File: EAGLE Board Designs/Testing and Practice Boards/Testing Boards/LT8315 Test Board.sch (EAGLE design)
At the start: 21 parts, among them T1 TRANSFORMER(3W), U1 LT8315

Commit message: Finished schem and started board
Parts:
- added C10, C9: CAPACITOR_1206_25V_33UF, HyTechDevices:CAPACITOR_1206_25V_33UF
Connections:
- net N$15: now also C10.1, C9.1
- net N$16: now also C10.2, C9.2
- net N$2: no longer C8.2
- net TS-UNFUSED: now also C8.2
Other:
- moved on the sheet: C8
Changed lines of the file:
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@@
 <part name="C7" library="HyTechDevices" deviceset="CAPACITOR_?_*" device="0603" technology="100V_0.1UF"/>
 <part name="C8" library="HyTechDevices" deviceset="CAPACITOR_?_*" device="" technology="0.1UF"/>
+<part name="C9" library="HyTechDevices" deviceset="CAPACITOR_?_*" device="1206" technology="25V_33UF"/>
+<part name="C10" library="HyTechDevices" deviceset="CAPACITOR_?_*" device="1206" technology="25V_33UF"/>
+<part name="P4" library="HyTechSupplies" deviceset="TS+UNFUSED" device=""/>
+<part name="P5" library="HyTechSupplies" deviceset="TS-UNFUSED" device=""/>
 </parts>
 <sheets>
@@
 <attribute name="CAPACITANCE" x="249.428" y="142.24" size="1.27" layer="96" rot="R90" align="top-center"/>
 </instance>
-<instance part="C8" gate="G$1" x="186.69" y="138.43" smashed="yes" rot="R90">
-<attribute name="NAME" x="184.15" y="137.16" size="1.27" layer="95" rot="R90" align="bottom-center"/>
+<instance part="C8" gate="G$1" x="60.96" y="139.7" smashed="yes" rot="R90">
+<attribute name="NAME" x="58.42" y="138.43" size="1.27" layer="95" rot="R90" align="bottom-center"/>
+</instance>
+<instance part="C9" gate="G$1" x="255.27" y="143.51" smashed="yes" rot="R90">
+<attribute name="NAME" x="252.73" y="142.24" size="1.27" layer="95" rot="R90" align="bottom-center"/>
+<attribute name="VOLTAGE" x="257.81" y="142.24" size="1.27" layer="96" rot="R90" align="top-center"/>
+<attribute name="CAPACITANCE" x="259.588" y="142.24" size="1.27" layer="96" rot="R90" align="top-center"/>
+</instance>
+<instance part="C10" gate="G$1" x="265.43" y="143.51" smashed="yes" rot="R90">
+<attribute name="NAME" x="262.89" y="142.24" size="1.27" layer="95" rot="R90" align="bottom-center"/>
+<attribute name="VOLTAGE" x="267.97" y="142.24" size="1.27" layer="96" rot="R90" align="top-center"/>
+<attribute name="CAPACITANCE" x="269.748" y="142.24" size="1.27" layer="96" rot="R90" align="top-center"/>
+</instance>
+<instance part="P4" gate="G$1" x="60.96" y="147.32" smashed="yes">
+<attribute name="VALUE" x="60.96" y="152.4" size="1.27" layer="96" align="bottom-center"/>
+</instance>
+<instance part="P5" gate="G$1" x="60.96" y="129.54" smashed="yes">
+<attribute name="VALUE" x="60.96" y="127" size="1.27" layer="96" align="top-center"/>
 </instance>
 </instances>
@@
 <wire x1="177.8" y1="132.08" x2="156.21" y2="132.08" width="0.1524" layer="91"/>
 <junction x="177.8" y="132.08"/>
-<pinref part="C8" gate="G$1" pin="2"/>
-<wire x1="186.69" y1="133.35" x2="186.69" y2="132.08" width="0.1524" layer="91"/>
-<junction x="186.69" y="132.08"/>
 </segment>
 </net>
@@
 <wire x1="182.88" y1="142.24" x2="186.69" y2="142.24" width="0.1524" layer="91"/>
 <pinref part="T1" gate="G$1" pin="3"/>
+<wire x1="186.69" y1="142.24" x2="189.23" y2="142.24" width="0.1524" layer="91"/>
+</segment>
+<segment>
+<pinref part="P4" gate="G$1" pin="TS+UNFUSED"/>
 <pinref part="C8" gate="G$1" pin="1"/>
-<wire x1="186.69" y1="142.24" x2="189.23" y2="142.24" width="0.1524" layer="91"/>
-<wire x1="186.69" y1="140.97" x2="186.69" y2="142.24" width="0.1524" layer="91"/>
-<junction x="186.69" y="142.24"/>
+<wire x1="60.96" y1="142.24" x2="60.96" y2="144.78" width="0.1524" layer="91"/>
 </segment>
 </net>
@@
 <wire x1="171.45" y1="157.48" x2="184.15" y2="157.48" width="0.1524" layer="91"/>
 </segment>
+<segment>
+<pinref part="P5" gate="G$1" pin="TS-UNFUSED"/>
+<pinref part="C8" gate="G$1" pin="2"/>
+<wire x1="60.96" y1="132.08" x2="60.96" y2="134.62" width="0.1524" layer="91"/>
+</segment>
 </net>
 <net name="N$4" class="0">
@@
 <wire x1="245.11" y1="147.32" x2="245.11" y2="146.05" width="0.1524" layer="91"/>
 <junction x="234.95" y="147.32"/>
+<pinref part="C9" gate="G$1" pin="1"/>
+<wire x1="245.11" y1="147.32" x2="255.27" y2="147.32" width="0.1524" layer="91"/>
+<wire x1="255.27" y1="147.32" x2="255.27" y2="146.05" width="0.1524" layer="91"/>
+<junction x="245.11" y="147.32"/>
+<pinref part="C10" gate="G$1" pin="1"/>
+<wire x1="255.27" y1="147.32" x2="265.43" y2="147.32" width="0.1524" layer="91"/>
+<wire x1="265.43" y1="147.32" x2="265.43" y2="146.05" width="0.1524" layer="91"/>
+<junction x="255.27" y="147.32"/>
 </segment>
 </net>
@@
 <wire x1="245.11" y1="137.16" x2="234.95" y2="137.16" width="0.1524" layer="91"/>
 <junction x="234.95" y="137.16"/>
-</segment>
-</net>
+<pinref part="C9" gate="G$1" pin="2"/>
+<wire x1="245.11" y1="137.16" x2="255.27" y2="137.16" width="0.1524" layer="91"/>
+<wire x1="255.27" y1="137.16" x2="255.27" y2="138.43" width="0.1524" layer="91"/>
+<junction x="245.11" y="137.16"/>
+<pinref part="C10" gate="G$1" pin="2"/>
+<wire x1="255.27" y1="137.16" x2="265.43" y2="137.16" width="0.1524" layer="91"/>
+<wire x1="265.43" y1="137.16" x2="265.43" y2="138.43" width="0.1524" layer="91"/>
+<junction x="255.27" y="137.16"/>
+</segment>
+</net>

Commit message: Made more changes to board and schematic
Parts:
- added D5: LED_0603_GREEN, HyTechDevices:LED_0603_GREEN
- added J1, J2: CONNECTOR-2_μF_T_V_BLACK, HyTechDevices:CONNECTOR-2_μF_T_V_BLACK
- added R8: RESISTOR_0603_1K, HyTechDevices:RESISTOR_0603_1K
- added TP1, TP2, TP3, TP4, TP5: TEST_POINT, HyTechDevices:TEST_POINT
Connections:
- removed net N$16: C10.2, C6.2, C7.2, C9.2, T1.10,11
- new net +5V: C10.1, C6.1, C7.1, C9.1, D4.C, J2.1, R8.2, TP4.1
- new net GND: C10.2, C6.2, C7.2, C9.2, D5.C, J2.2, T1.10,11, TP5.1
- net N$15: now also D5.A, R8.1; no longer C10.1, C6.1, C7.1, C9.1, D4.C
- net N$9: now also TP1.1
- net TS+UNFUSED: now also J1.1, TP2.1
- net TS-UNFUSED: now also J1.2, TP3.1
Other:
- moved on the sheet: C1, C10, C2, C3, C4, C5, C6, C7, C8, C9, D1, D2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

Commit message: Added BOMs and finished board
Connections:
- net +5V renamed +12V
- net N$9 renamed AUX
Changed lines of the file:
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@@
 <part name="U1" library="HyTechDevices" deviceset="LT8315" device=""/>
 <part name="D1" library="HyTechDevices" deviceset="TVS_*" device="SOD323F"/>
-<part name="D2" library="HyTechDevices" deviceset="RECTIFIER_*_?" device="SMA"/>
 <part name="T1" library="HyTechDevices" deviceset="TRANSFORMER(3W)" device=""/>
 <part name="P1" library="HyTechSupplies" deviceset="TS-UNFUSED" device=""/>
@@
 <part name="TP4" library="HyTechDevices" deviceset="TEST_POINT" device=""/>
 <part name="TP5" library="HyTechDevices" deviceset="TEST_POINT" device=""/>
-<part name="P6" library="HyTechSupplies" deviceset="+5V" device=""/>
 <part name="P7" library="HyTechSupplies" deviceset="GND" device=""/>
-<part name="P8" library="HyTechSupplies" deviceset="+5V" device=""/>
 <part name="P9" library="HyTechSupplies" deviceset="GND" device=""/>
 <part name="R8" library="HyTechDevices" deviceset="RESISTOR_?_*" device="0603" technology="1K"/>
 <part name="D5" library="HyTechDevices" deviceset="LED_?_*" device="0603" technology="GREEN"/>
+<part name="P6" library="HyTechSupplies" deviceset="+12V" device=""/>
+<part name="P8" library="HyTechSupplies" deviceset="+12V" device=""/>
+<part name="D2" library="HyTechDevices" deviceset="RECTIFIER_*_?" device="SMA"/>
 </parts>
 <sheets>
@@
 <attribute name="VOLTAGE" x="147.955" y="140.97" size="1.27" layer="96" rot="R270" align="top-center"/>
 </instance>
-<instance part="D2" gate="G$1" x="149.86" y="134.62" smashed="yes" rot="R90">
-<attribute name="NAME" x="147.955" y="133.35" size="1.27" layer="95" rot="R90" align="bottom-center"/>
-<attribute name="MPN" x="153.67" y="133.35" size="1.27" layer="96" rot="R90" align="top-center"/>
-</instance>
 <instance part="T1" gate="G$1" x="173.99" y="139.7" smashed="yes">
 <attribute name="NAME" x="173.99" y="150.622" size="1.27" layer="95" align="bottom-center"/>
@@
 <attribute name="MPN" x="245.618" y="129.54" size="1.27" layer="95" rot="R90" align="top-left"/>
 </instance>
-<instance part="P6" gate="1" x="217.17" y="147.32" smashed="yes">
-<attribute name="VALUE" x="217.17" y="149.86" size="1.27" layer="96" align="bottom-center"/>
-</instance>
 <instance part="P7" gate="1" x="217.17" y="132.08" smashed="yes">
 <attribute name="VALUE" x="217.17" y="130.81" size="1.27" layer="96" align="top-center"/>
-</instance>
-<instance part="P8" gate="1" x="217.17" y="124.46" smashed="yes">
-<attribute name="VALUE" x="217.17" y="127" size="1.27" layer="96" align="bottom-center"/>
 </instance>
 <instance part="P9" gate="1" x="217.17" y="104.14" smashed="yes">
@@
 <attribute name="COLOR" x="215.392" y="110.49" size="1.27" layer="95" rot="R270" align="top-center"/>
 <attribute name="NAME" x="220.726" y="110.49" size="1.27" layer="96" rot="R270" align="bottom-center"/>
+</instance>
+<instance part="P6" gate="1" x="217.17" y="124.46" smashed="yes">
+<attribute name="VALUE" x="217.17" y="128.27" size="1.27" layer="96" align="bottom-center"/>
+</instance>
+<instance part="P8" gate="1" x="217.17" y="147.066" smashed="yes">
+<attribute name="VALUE" x="217.17" y="150.876" size="1.27" layer="96" align="bottom-center"/>
+</instance>
+<instance part="D2" gate="G$1" x="149.86" y="134.62" smashed="yes" rot="R90">
+<attribute name="NAME" x="147.955" y="133.35" size="1.27" layer="95" rot="R90" align="bottom-center"/>
+<attribute name="VOLTAGE" x="151.765" y="133.35" size="1.27" layer="96" rot="R90" align="top-center"/>
+<attribute name="MPN" x="153.67" y="133.35" size="1.27" layer="96" rot="R90" align="top-center"/>
 </instance>
 </instances>
@@
 </busses>
 <nets>
-<net name="N$1" class="0">
-<segment>
-<pinref part="D2" gate="G$1" pin="C"/>
-<pinref part="D1" gate="G$1" pin="C"/>
-</segment>
-</net>
 <net name="N$2" class="0">
 <segment>
 <pinref part="T1" gate="G$1" pin="1"/>
-<pinref part="D2" gate="G$1" pin="A"/>
 <pinref part="U1" gate="G$1" pin="DRAIN"/>
 <wire x1="161.29" y1="129.54" x2="149.86" y2="129.54" width="0.1524" layer="91"/>
+<pinref part="D2" gate="G$1" pin="A"/>
 <wire x1="149.86" y1="129.54" x2="128.27" y2="129.54" width="0.1524" layer="91"/>
 <junction x="149.86" y="129.54"/>
@@
 </segment>
 </net>
-<net name="N$9" class="0">
+<net name="AUX" class="0">
 <segment>
 <pinref part="C2" gate="G$1" pin="1"/>
@@
 <pinref part="D4" gate="G$1" pin="A"/>
 <wire x1="186.69" y1="144.78" x2="190.5" y2="144.78" width="0.1524" layer="91"/>
-</segment>
-</net>
-<net name="+5V" class="0">
-<segment>
-<pinref part="D4" gate="G$1" pin="C"/>
-<pinref part="C6" gate="G$1" pin="1"/>
-<wire x1="198.12" y1="144.78" x2="207.01" y2="144.78" width="0.1524" layer="91"/>
-<wire x1="207.01" y1="144.78" x2="207.01" y2="143.51" width="0.1524" layer="91"/>
-<pinref part="C7" gate="G$1" pin="1"/>
-<wire x1="207.01" y1="144.78" x2="217.17" y2="144.78" width="0.1524" layer="91"/>
-<wire x1="217.17" y1="144.78" x2="217.17" y2="143.51" width="0.1524" layer="91"/>
-<junction x="207.01" y="144.78"/>
-<pinref part="C9" gate="G$1" pin="1"/>
-<wire x1="217.17" y1="144.78" x2="227.33" y2="144.78" width="0.1524" layer="91"/>
-<wire x1="227.33" y1="144.78" x2="227.33" y2="143.51" width="0.1524" layer="91"/>
-<junction x="217.17" y="144.78"/>
-<pinref part="C10" gate="G$1" pin="1"/>
-<wire x1="227.33" y1="144.78" x2="236.22" y2="144.78" width="0.1524" layer="91"/>
-<wire x1="236.22" y1="144.78" x2="237.49" y2="144.78" width="0.1524" layer="91"/>
-<wire x1="237.49" y1="144.78" x2="237.49" y2="143.51" width="0.1524" layer="91"/>
-<junction x="227.33" y="144.78"/>
-<pinref part="J2" gate="G$1" pin="1"/>
-<wire x1="246.38" y1="139.7" x2="243.84" y2="139.7" width="0.1524" layer="91"/>
-<wire x1="243.84" y1="139.7" x2="243.84" y2="144.78" width="0.1524" layer="91"/>
-<wire x1="243.84" y1="144.78" x2="237.49" y2="144.78" width="0.1524" layer="91"/>
-<pinref part="TP4" gate="G$1" pin="1"/>
-<junction x="243.84" y="144.78"/>
-<pinref part="P6" gate="1" pin="+5V"/>
-</segment>
-<segment>
-<pinref part="P8" gate="1" pin="+5V"/>
-<pinref part="R8" gate="G$1" pin="2"/>
 </segment>
 </net>
@@
 </segment>
 </net>
+<net name="+12V" class="0">
+<segment>
+<pinref part="R8" gate="G$1" pin="2"/>
+<pinref part="P6" gate="1" pin="+12V"/>
+</segment>
+<segment>
+<pinref part="D4" gate="G$1" pin="C"/>
+<pinref part="C6" gate="G$1" pin="1"/>
+<wire x1="198.12" y1="144.78" x2="207.01" y2="144.78" width="0.1524" layer="91"/>
+<wire x1="207.01" y1="144.78" x2="207.01" y2="143.51" width="0.1524" layer="91"/>
+<pinref part="C7" gate="G$1" pin="1"/>
+<wire x1="207.01" y1="144.78" x2="217.17" y2="144.78" width="0.1524" layer="91"/>
+<wire x1="217.17" y1="144.78" x2="217.17" y2="144.526" width="0.1524" layer="91"/>
+<junction x="207.01" y="144.78"/>
+<pinref part="C9" gate="G$1" pin="1"/>
+<wire x1="217.17" y1="144.526" x2="217.17" y2="143.51" width="0.1524" layer="91"/>
+<wire x1="217.17" y1="144.78" x2="227.33" y2="144.78" width="0.1524" layer="91"/>
+<wire x1="227.33" y1="144.78" x2="227.33" y2="143.51" width="0.1524" layer="91"/>
+<junction x="217.17" y="144.78"/>
+<pinref part="C10" gate="G$1" pin="1"/>
+<wire x1="227.33" y1="144.78" x2="237.49" y2="144.78" width="0.1524" layer="91"/>
+<wire x1="237.49" y1="144.78" x2="237.49" y2="143.51" width="0.1524" layer="91"/>
+<junction x="227.33" y="144.78"/>
+<pinref part="J2" gate="G$1" pin="1"/>
+<wire x1="246.38" y1="139.7" x2="243.84" y2="139.7" width="0.1524" layer="91"/>
+<wire x1="243.84" y1="139.7" x2="243.84" y2="144.78" width="0.1524" layer="91"/>
+<wire x1="243.84" y1="144.78" x2="237.49" y2="144.78" width="0.1524" layer="91"/>
+<pinref part="TP4" gate="G$1" pin="1"/>
+<junction x="243.84" y="144.78"/>
+<pinref part="P8" gate="1" pin="+12V"/>
+<junction x="217.17" y="144.526"/>
+</segment>
+</net>
+<net name="N$1" class="0">
+<segment>
+<pinref part="D1" gate="G$1" pin="C"/>
+<pinref part="D2" gate="G$1" pin="C"/>
+</segment>
+</net>

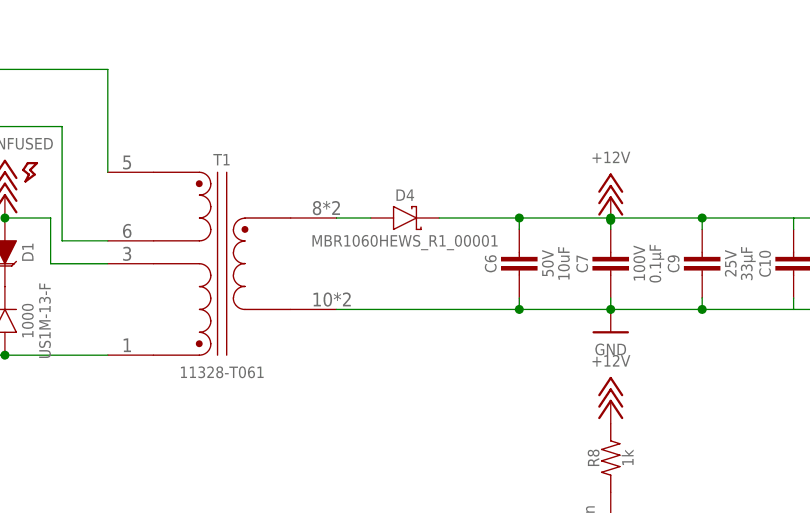
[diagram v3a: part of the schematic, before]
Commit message: changed to 400V diode
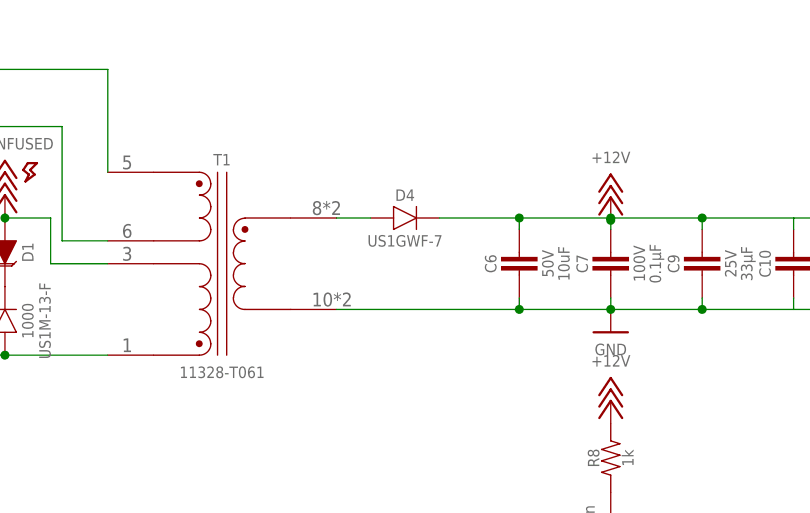
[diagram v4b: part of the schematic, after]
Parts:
- D4: value SCHOTTKY_SOD323_60V -> RECTIFIER_400V_SOD123; device HyTechDevices:SCHOTTKY_SOD323_60V -> HyTechDevices:RECTIFIER_400V_SOD123
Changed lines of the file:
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@@
 <part name="C5" library="HyTechDevices" deviceset="CAPACITOR_?_*" device="0603" technology="25V_10UF"/>
 <part name="R7" library="HyTechDevices" deviceset="RESISTOR_?_*" device="0603" technology="0.5"/>
-<part name="D4" library="HyTechDevices" deviceset="SCHOTTKY_?_*" device="SOD323" technology="60V"/>
+<part name="D4" library="HyTechDevices" deviceset="RECTIFIER_*_?" device="SOD123" technology="400V"/>
 <part name="C6" library="HyTechDevices" deviceset="CAPACITOR_?_*" device="0805" technology="50V_10UF"/>
 <part name="C7" library="HyTechDevices" deviceset="CAPACITOR_?_*" device="0603" technology="100V_0.1UF"/>
